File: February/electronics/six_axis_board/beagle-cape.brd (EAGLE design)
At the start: 180 x 128 mm, 74 parts, among them IC1 74HCT244DW, IC2 74HCT244DW, IC3 74HCT244DW, IC4 LM2574M-5.0, Q1 BSS123

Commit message: more routing; auto the rest
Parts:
- moved IC3 9.24 mm to (145.5, 52.5)
- moved C1 8.07 mm to (146.0, 41.0)
- moved IC2 0.97 mm to (89.0, 60.5)
- moved C2 0.71 mm to (88.5, 46.7)
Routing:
- net GND: track 483.5 -> 624.0 mm
- net VCC: track 61.8 -> 108.1 mm
- net N$61: track 0.00 -> 41.5 mm
- net N$47: track 0.00 -> 35.8 mm
- net N$41: track 0.00 -> 35.7 mm
- net N$27: track 0.00 -> 32.8 mm
- net N$60: track 0.00 -> 32.3 mm
- net N$18: track 0.00 -> 32.1 mm
- net N$4: track 0.00 -> 31.0 mm
- net N$59: track 0.00 -> 29.4 mm
- net N$48: track 0.00 -> 28.7 mm
- net N$49: track 0.00 -> 24.8 mm
- net N$40: track 0.00 -> 24.5 mm
- net N$28: track 0.00 -> 20.9 mm
- net N$17: track 0.00 -> 20.5 mm
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
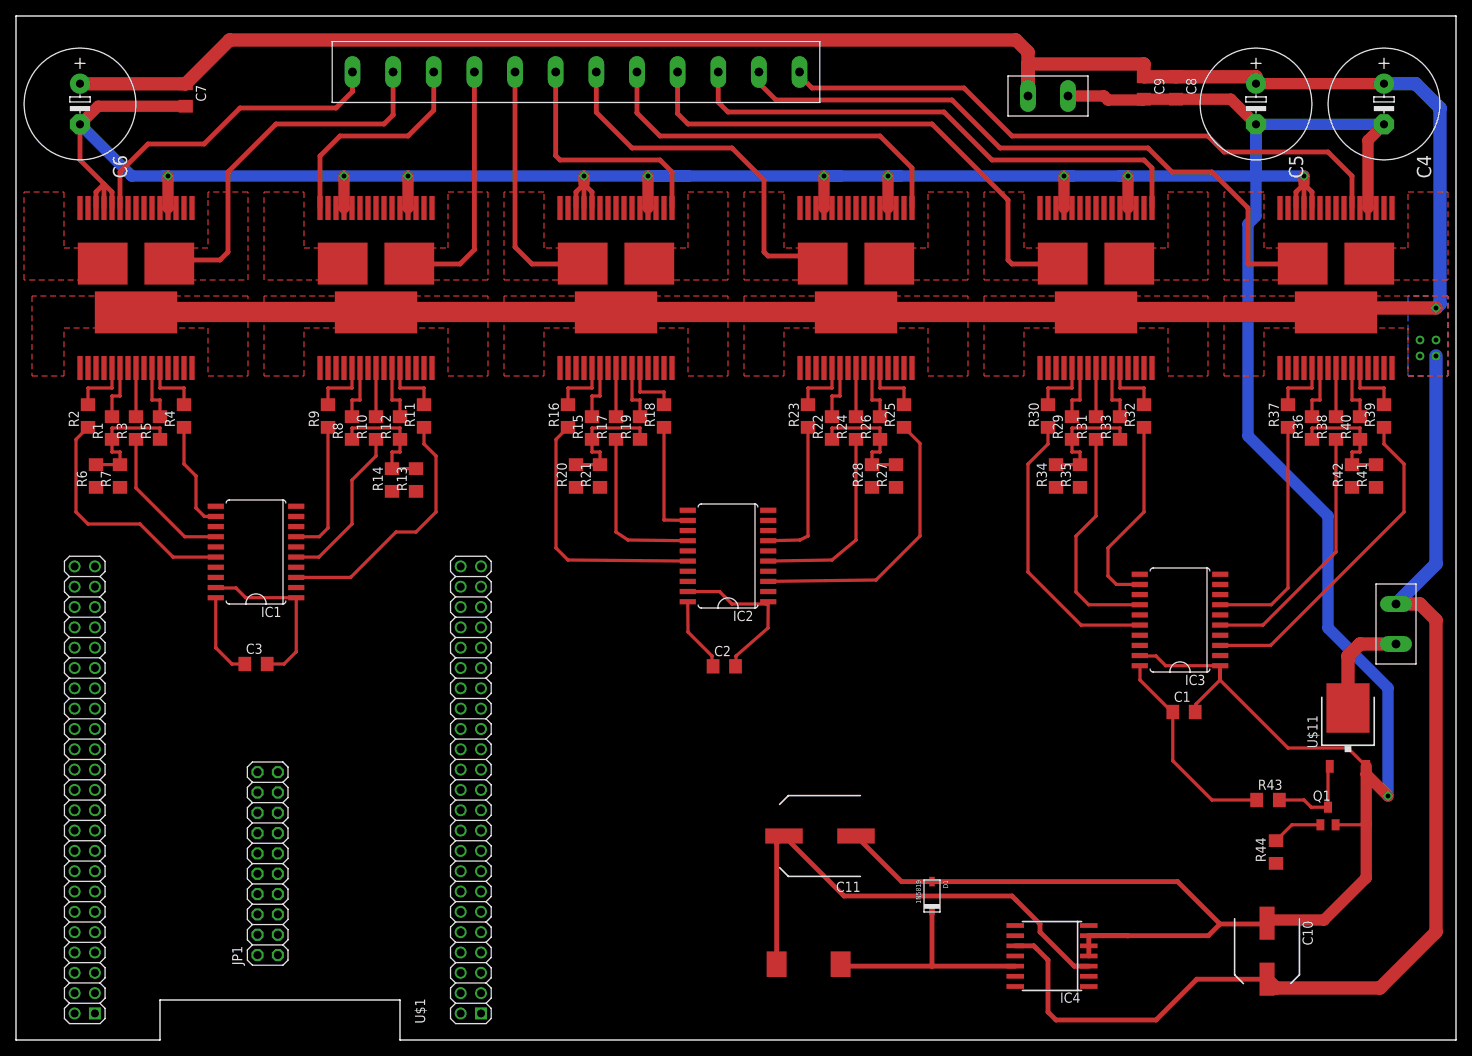
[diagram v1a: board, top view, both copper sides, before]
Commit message: board layout is pretty much done and doc strings are in. prepping for production.
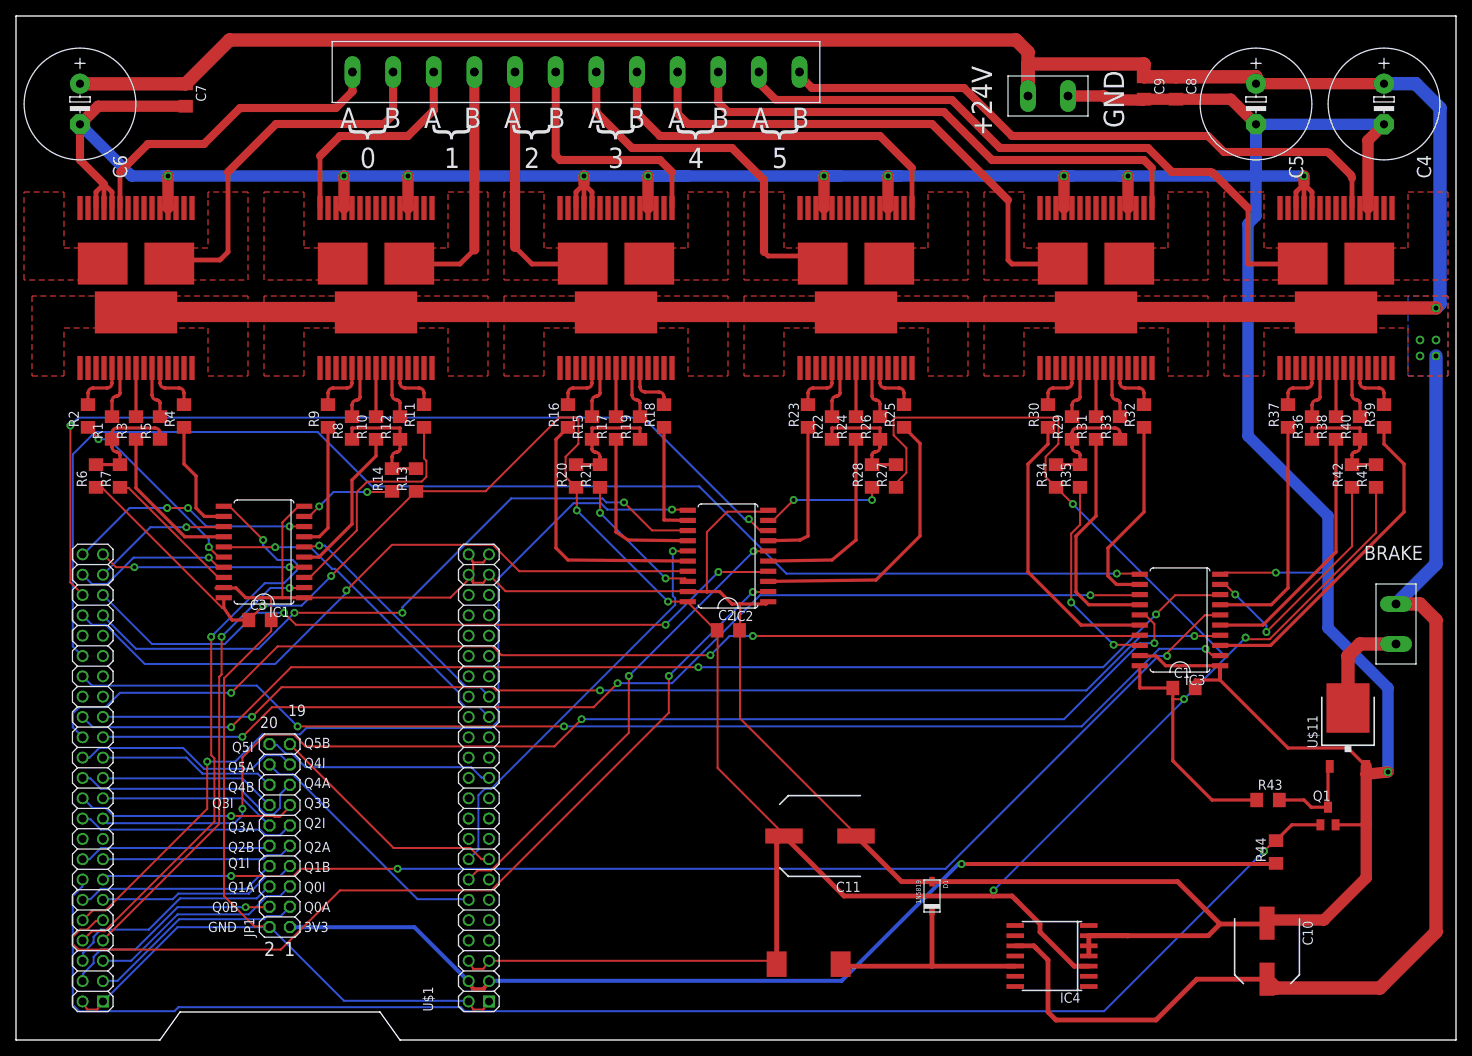
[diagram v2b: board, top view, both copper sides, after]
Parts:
- moved C3 5.52 mm to (30.5, 52.5)
- moved C2 4.53 mm to (89.0, 51.2)
- moved JP1 3.81 mm to (33.0, 25.6)
- moved C1 3.00 mm to (146.0, 44.0)
- moved U$1 1.80 mm to (6.42, -14.2)
- moved IC1 1.00 mm to (31.0, 61.0)
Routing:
- net VCC: track 108.1 -> 419.6 mm, vias 0 -> 8
- net GND: track 624.0 -> 844.6 mm, vias 11 -> 12
- net BRAKE: track 6.37 -> 182.5 mm, vias 0 -> 1
- net EN5: track 0.00 -> 167.6 mm, vias 0 -> 1
- net PWM4: track 0.00 -> 153.6 mm, vias 0 -> 3
- net PWM5: track 0.00 -> 151.2 mm, vias 0 -> 3
- net IN4B: track 0.00 -> 149.6 mm, vias 0 -> 3
- net EN4: track 0.00 -> 149.2 mm, vias 0 -> 3
- net IN4A: track 0.00 -> 144.3 mm, vias 0 -> 3
- net IN5B: track 0.00 -> 141.8 mm, vias 0 -> 3
- net IN5A: track 0.00 -> 137.0 mm, vias 0 -> 3
- net +3V3: track 0.00 -> 133.3 mm, vias 0 -> 1
- net IN2B: track 0.00 -> 115.3 mm, vias 0 -> 2
- net EN2: track 0.00 -> 114.0 mm, vias 0 -> 2
- net EN3: track 0.00 -> 111.5 mm, vias 0 -> 2
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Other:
- outline, holes or cut-outs redrawn
- board text added: "+24V"
- board text added: "0"
- board text added: "1"
- board text added: "19"
- board text added: "2"
- board text added: "20"
- board text added: "3"
- board text added: "3V3"
- board text added: "4"
- board text added: "5"
- board text added: "A"
- board text added: "B"
- board text added: "BRAKE"
- board text added: "GND"
- board text added: "Q0A"
- board text added: "Q0B"
- board text added: "Q0I"
- board text added: "Q1A"
- board text added: "Q1B"
- board text added: "Q1I"
- board text added: "Q2A"
- board text added: "Q2B"
- board text added: "Q2I"
- board text added: "Q3A"
- board text added: "Q3B"
- board text added: "Q3I"
- board text added: "Q4A"
- board text added: "Q4B"
- board text added: "Q4I"
- board text added: "Q5A"
- board text added: "Q5B"
- board text added: "Q5I"
- board text added: "{"
